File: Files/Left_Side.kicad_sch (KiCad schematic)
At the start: 76 parts, among them J1 USB_C_Receptacle, J3 USB_C_Receptacle, U1 W25Q128JVS, U2 XC6206-3.3_SOT, U3 USBLC6-2SC6, U4 RP2040, Y1 Crystal_GND24

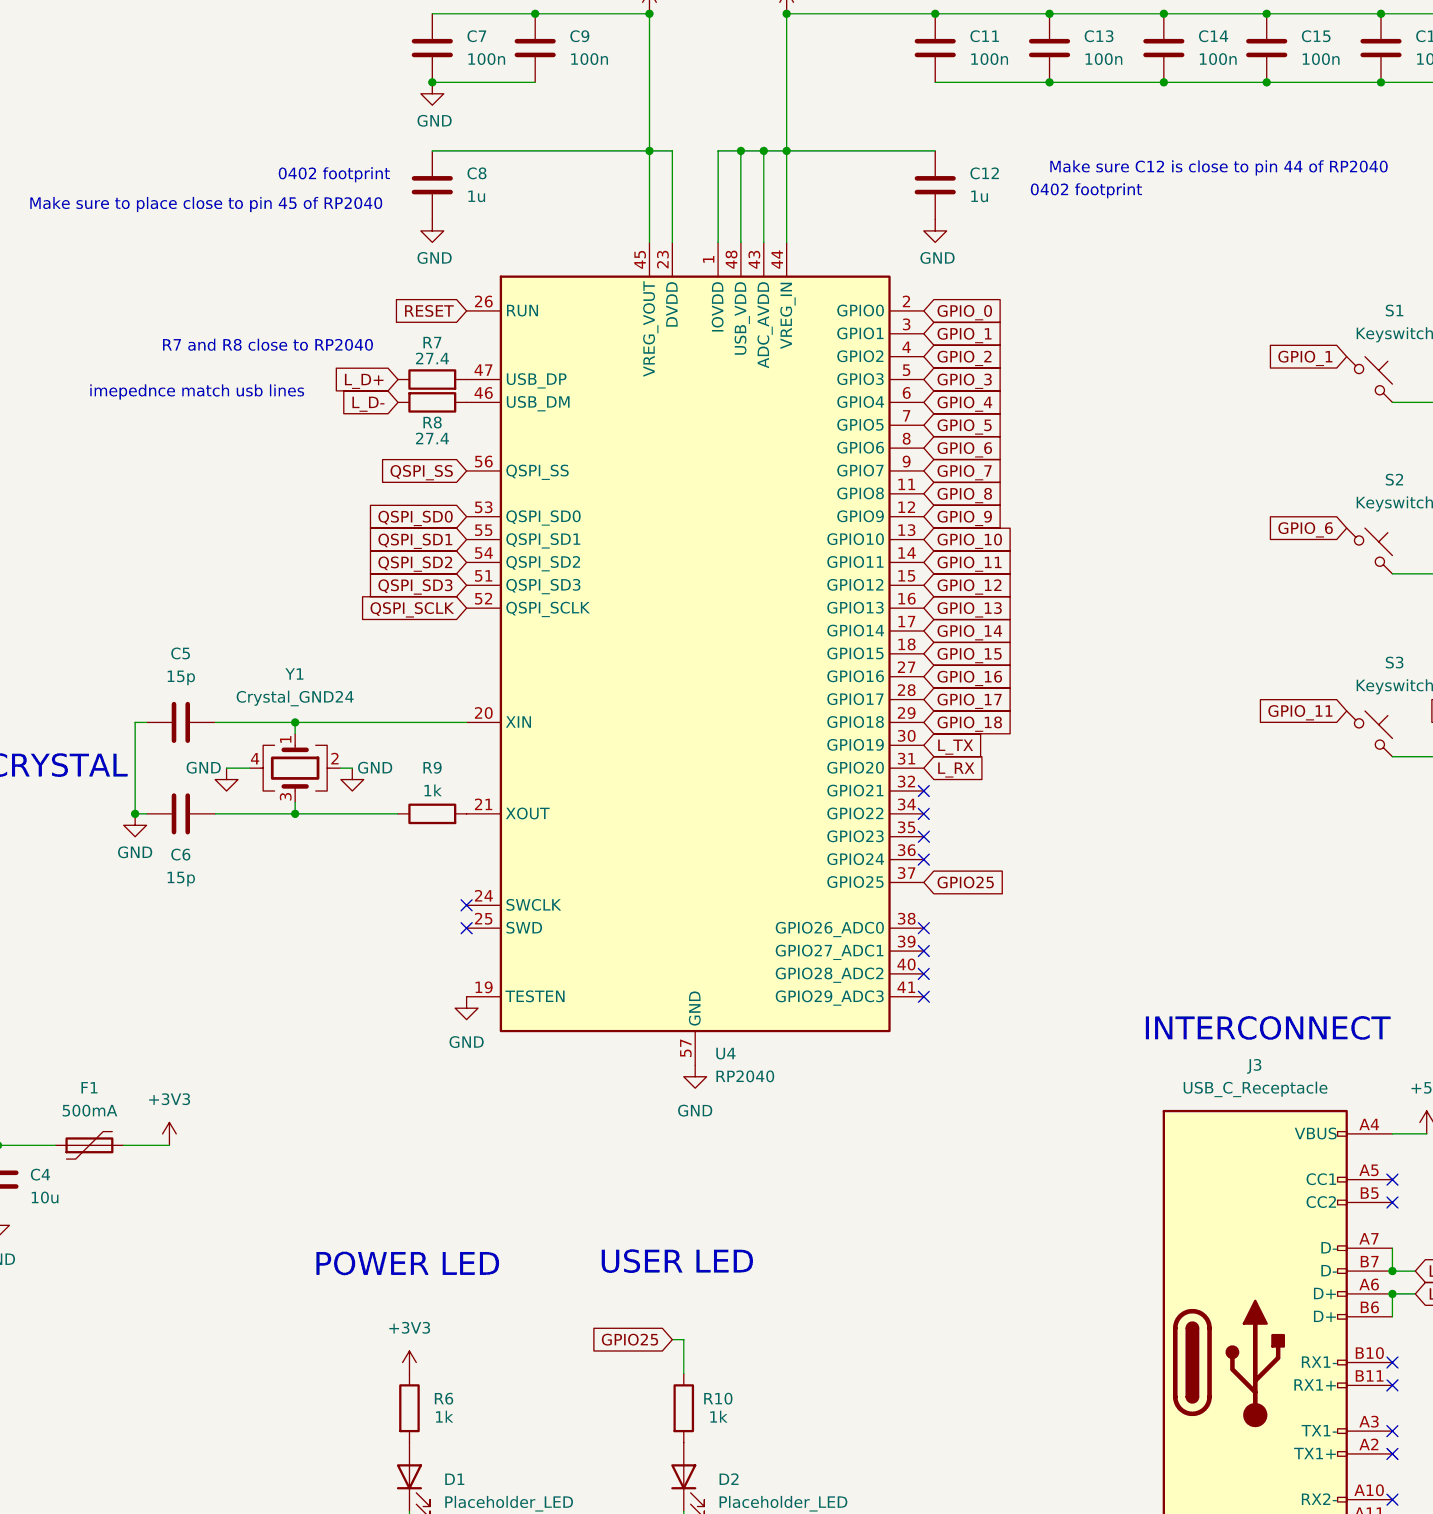
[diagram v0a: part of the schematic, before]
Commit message: placed companets and semi routed
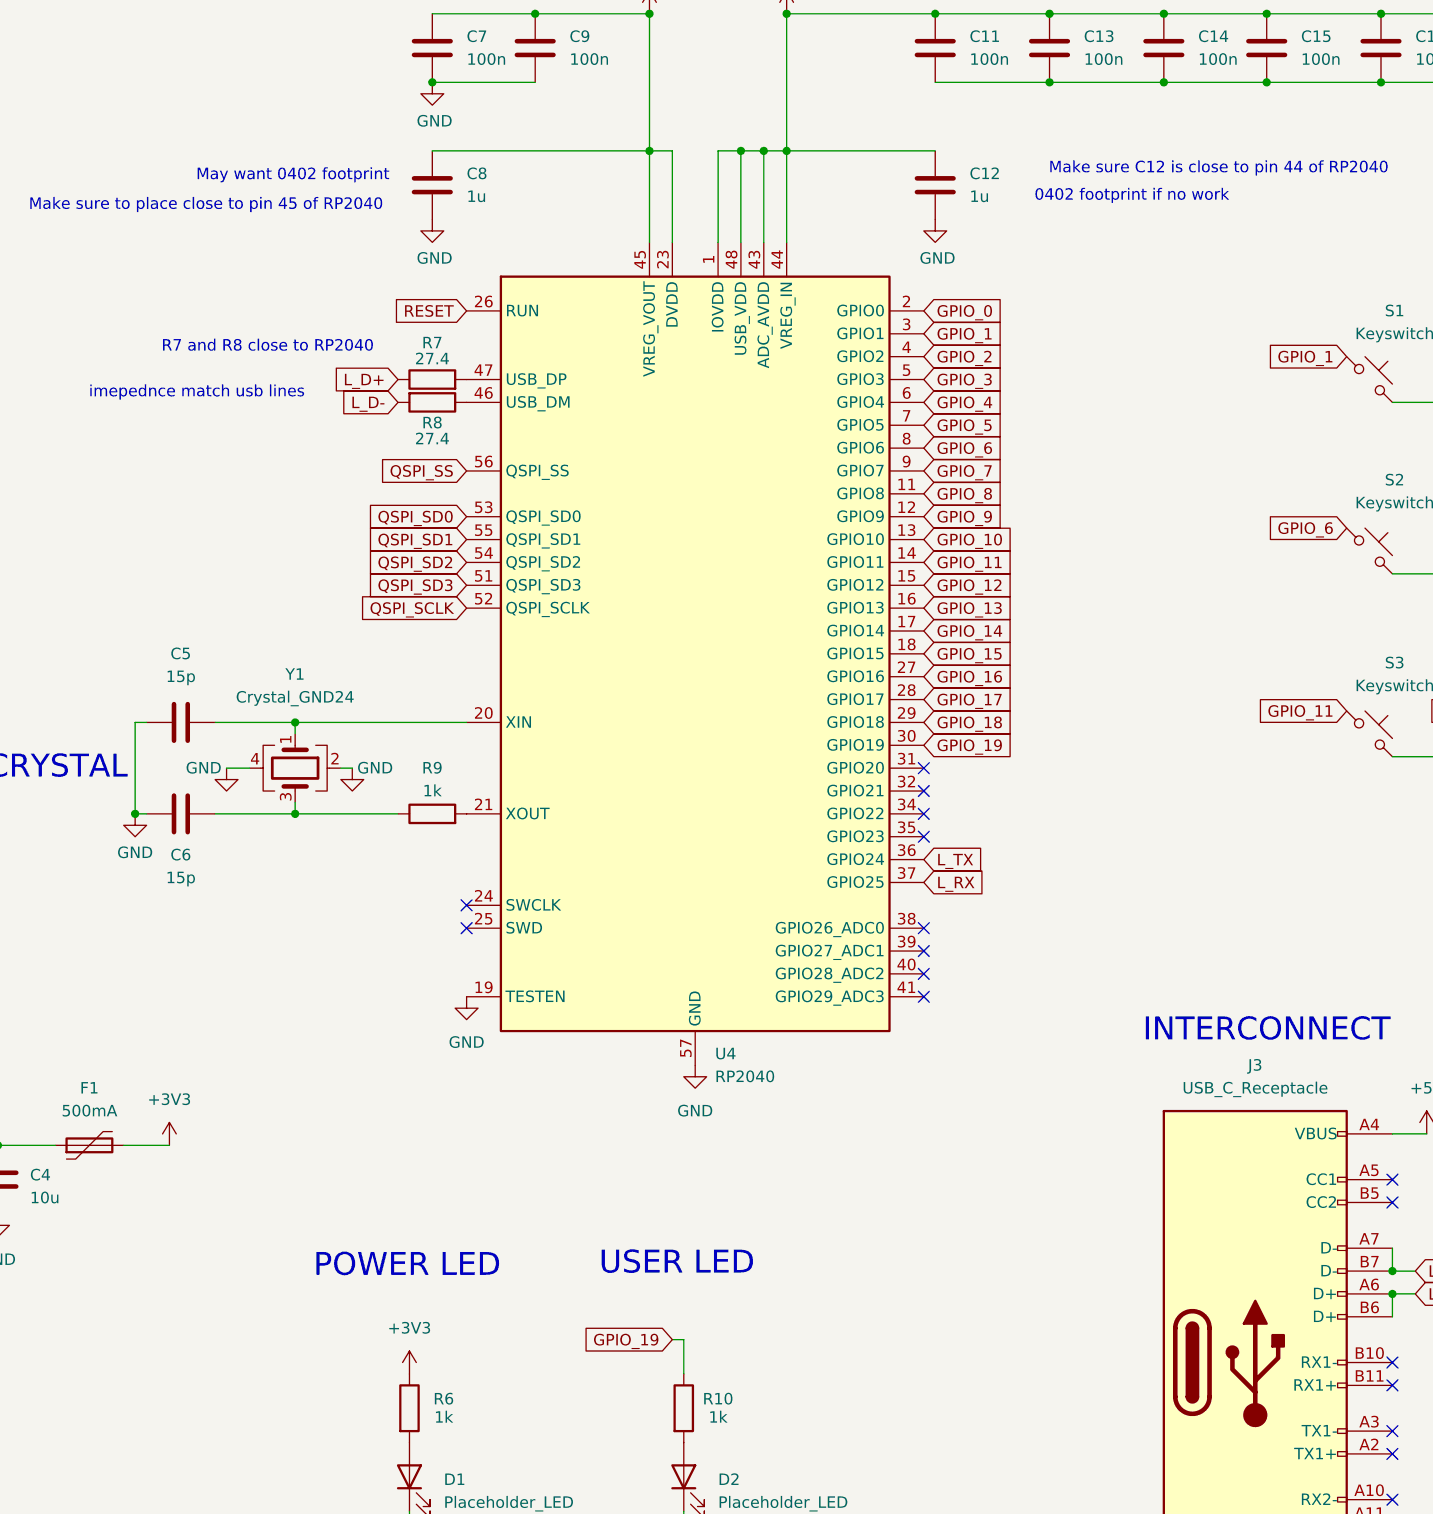
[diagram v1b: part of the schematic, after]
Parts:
- C1, C10, C11, C13, C14, C15, C16, C17, C18, C2, C3, C4, C5, C6, C7, C9: footprint ScottoKeebs_Components:Capacitor_0603 -> Capacitor_SMD:C_0805_2012Metric_Pad1.18x1.45mm_HandSolder
- C12, C8: footprint ScottoKeebs_Components:Capacitor_0402 -> Capacitor_SMD:C_0805_2012Metric_Pad1.18x1.45mm_HandSolder
- R1, R10, R2, R3, R4, R5, R6, R7, R8, R9: footprint Resistor_SMD:R_0603_1608Metric -> Resistor_SMD:R_0805_2012Metric_Pad1.20x1.40mm_HandSolder
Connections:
- net L_RX: now also U4.37 (GPIO25); no longer U4.31 (GPIO20)
- net L_TX: now also U4.36 (GPIO24); no longer U4.30 (GPIO19)
- net GPIO25 renamed GPIO_19
- net GPIO_19: now also U4.30 (GPIO19); no longer U4.37 (GPIO25)
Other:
- note added: "0402 footprint if no work"
- note added: "May want 0402 footprint"
- note removed: "0402 footprint"
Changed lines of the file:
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@@
 	)
 	(no_connect
-		(at 240.03 147.32)
-	)
-	(no_connect
 		(at 292.1 220.98)
 	)
@@
 	)
 	(no_connect
+		(at 240.03 137.16)
+	)
+	(no_connect
 		(at 83.82 234.95)
 	)
@@
 		)
 	)
-	(text "0402 footprint\n"
+	(text "May want 0402 footprint\n"
 		(exclude_from_sim no)
-		(at 174.498 71.374 0)
+		(at 169.926 71.374 0)
 		(effects
 			(font
@@
 		)
 	)
-	(text "0402 footprint\n"
+	(text "0402 footprint if no work\n"
 		(exclude_from_sim no)
-		(at 258.064 73.152 0)
+		(at 263.144 73.66 0)
 		(effects
 			(font
@@
 		)
 	)
-	(global_label "GPIO25"
+	(global_label "GPIO_19"
 		(shape input)
-		(at 240.03 149.86 0)
+		(at 240.03 134.62 0)
 		(fields_autoplaced yes)
 		(effects
@@
 		)
 		(property "Intersheetrefs" "${INTERSHEET_REFS}"
-			(at 249.9095 149.86 0)
+			(at 250.8771 134.62 0)
 			(effects
 				(font
@@
 		)
 	)
-	(global_label "GPIO25"
+	(global_label "GPIO_19"
 		(shape input)
 		(at 212.09 200.66 180)
@@
 		)
 		(property "Intersheetrefs" "${INTERSHEET_REFS}"
-			(at 202.2105 200.66 0)
+			(at 201.2429 200.66 0)
 			(effects
 				(font
@@
 	(global_label "L_TX"
 		(shape input)
-		(at 240.03 134.62 0)
+		(at 240.03 147.32 0)
 		(fields_autoplaced yes)
 		(effects
@@
 		)
 		(property "Intersheetrefs" "${INTERSHEET_REFS}"
-			(at 247.188 134.62 0)
+			(at 247.188 147.32 0)
 			(effects
 				(font
@@
 	(global_label "L_RX"
 		(shape input)
-		(at 240.03 137.16 0)
+		(at 240.03 149.86 0)
 		(fields_autoplaced yes)
 		(effects
@@
 		)
 		(property "Intersheetrefs" "${INTERSHEET_REFS}"
-			(at 247.4904 137.16 0)
+			(at 247.4904 149.86 0)
 			(effects
 				(font
@@
 			)
 		)
-		(property "Footprint" "ScottoKeebs_Components:Capacitor_0603"
+		(property "Footprint" "Capacitor_SMD:C_0805_2012Metric_Pad1.18x1.45mm_HandSolder"
 			(at 153.67 133.0452 0)
 			(effects
@@
 			)
 		)
-		(property "Footprint" "Resistor_SMD:R_0603_1608Metric"
+		(property "Footprint" "Resistor_SMD:R_0805_2012Metric_Pad1.20x1.40mm_HandSolder"
 			(at 87.63 185.928 90)
 			(effects
@@
 			)
 		)
-		(property "Footprint" "ScottoKeebs_Components:Capacitor_0603"
+		(property "Footprint" "Capacitor_SMD:C_0805_2012Metric_Pad1.18x1.45mm_HandSolder"
 			(at 138.1252 186.69 0)
 			(effects
@@
 			)
 		)
-		(property "Footprint" "ScottoKeebs_Components:Capacitor_0603"
+		(property "Footprint" "Capacitor_SMD:C_0805_2012Metric_Pad1.18x1.45mm_HandSolder"
 			(at 84.1248 57.15 0)
 			(effects
@@
 			)
 		)
-		(property "Footprint" "Resistor_SMD:R_0603_1608Metric"
+		(property "Footprint" "Resistor_SMD:R_0805_2012Metric_Pad1.20x1.40mm_HandSolder"
 			(at 185.42 144.018 90)
 			(effects
@@
 			)
 		)
-		(property "Footprint" "ScottoKeebs_Components:Capacitor_0402"
+		(property "Footprint" "Capacitor_SMD:C_0805_2012Metric_Pad1.18x1.45mm_HandSolder"
 			(at 186.3852 76.2 0)
 			(effects
@@
 			)
 		)
-		(property "Footprint" "ScottoKeebs_Components:Capacitor_0603"
+		(property "Footprint" "Capacitor_SMD:C_0805_2012Metric_Pad1.18x1.45mm_HandSolder"
 			(at 279.0952 60.96 0)
 			(effects
@@
 			)
 		)
-		(property "Footprint" "ScottoKeebs_Components:Capacitor_0603"
+		(property "Footprint" "Capacitor_SMD:C_0805_2012Metric_Pad1.18x1.45mm_HandSolder"
 			(at 186.3852 60.96 0)
 			(effects
@@
 			)
 		)
-		(property "Footprint" "Resistor_SMD:R_0603_1608Metric"
+		(property "Footprint" "Resistor_SMD:R_0805_2012Metric_Pad1.20x1.40mm_HandSolder"
 			(at 185.42 95.758 90)
 			(effects
@@
 			)
 		)
-		(property "Footprint" "ScottoKeebs_Components:Capacitor_0603"
+		(property "Footprint" "Capacitor_SMD:C_0805_2012Metric_Pad1.18x1.45mm_HandSolder"
 			(at 121.92 105.7148 0)
 			(effects
@@
 			)
 		)
-		(property "Footprint" "ScottoKeebs_Components:Capacitor_0603"
+		(property "Footprint" "Capacitor_SMD:C_0805_2012Metric_Pad1.18x1.45mm_HandSolder"
 			(at 153.67 143.2052 0)
 			(effects
@@
 			)
 		)
-		(property "Footprint" "ScottoKeebs_Components:Capacitor_0603"
+		(property "Footprint" "Capacitor_SMD:C_0805_2012Metric_Pad1.18x1.45mm_HandSolder"
 			(at 318.4652 60.96 0)
 			(effects
@@
 			)
 		)
-		(property "Footprint" "ScottoKeebs_Components:Capacitor_0603"
+		(property "Footprint" "Capacitor_SMD:C_0805_2012Metric_Pad1.18x1.45mm_HandSolder"
 			(at 105.1052 186.69 0)
 			(effects
@@
 			)
 		)
-		(property "Footprint" "ScottoKeebs_Components:Capacitor_0603"
+		(property "Footprint" "Capacitor_SMD:C_0805_2012Metric_Pad1.18x1.45mm_HandSolder"
 			(at 304.4952 60.96 0)
 			(effects
@@
 			)
 		)
-		(property "Footprint" "ScottoKeebs_Components:Capacitor_0603"
+		(property "Footprint" "Capacitor_SMD:C_0805_2012Metric_Pad1.18x1.45mm_HandSolder"
 			(at 267.6652 60.96 0)
 			(effects
@@
 			)
 		)
-		(property "Footprint" "ScottoKeebs_Components:Capacitor_0603"
+		(property "Footprint" "Capacitor_SMD:C_0805_2012Metric_Pad1.18x1.45mm_HandSolder"
 			(at 254.9652 60.96 0)
 			(effects
@@
 			)
 		)
-		(property "Footprint" "ScottoKeebs_Components:Capacitor_0603"
+		(property "Footprint" "Capacitor_SMD:C_0805_2012Metric_Pad1.18x1.45mm_HandSolder"
 			(at 197.8152 60.96 0)
 			(effects
@@
 			)
 		)
-		(property "Footprint" "ScottoKeebs_Components:Capacitor_0402"
+		(property "Footprint" "Capacitor_SMD:C_0805_2012Metric_Pad1.18x1.45mm_HandSolder"
 			(at 242.2652 76.2 0)
 			(effects
@@
 			)
 		)
-		(property "Footprint" "ScottoKeebs_Components:Capacitor_0603"
+		(property "Footprint" "Capacitor_SMD:C_0805_2012Metric_Pad1.18x1.45mm_HandSolder"
 			(at 240.9952 41.91 0)
 			(effects
@@
 			)
 		)
-		(property "Footprint" "Resistor_SMD:R_0603_1608Metric"
+		(property "Footprint" "Resistor_SMD:R_0805_2012Metric_Pad1.20x1.40mm_HandSolder"
 			(at 185.42 94.742 90)
 			(effects
@@
 			)
 		)
-		(property "Footprint" "Resistor_SMD:R_0603_1608Metric"
+		(property "Footprint" "Resistor_SMD:R_0805_2012Metric_Pad1.20x1.40mm_HandSolder"
 			(at 87.63 188.468 90)
 			(effects
@@
 			)
 		)
-		(property "Footprint" "Resistor_SMD:R_0603_1608Metric"
+		(property "Footprint" "Resistor_SMD:R_0805_2012Metric_Pad1.20x1.40mm_HandSolder"
 			(at 95.758 110.49 90)
 			(effects
@@
 			)
 		)
-		(property "Footprint" "ScottoKeebs_Components:Capacitor_0603"
+		(property "Footprint" "Capacitor_SMD:C_0805_2012Metric_Pad1.18x1.45mm_HandSolder"
 			(at 291.7952 60.96 0)
 			(effects
@@
 			)
 		)
-		(property "Footprint" "Resistor_SMD:R_0603_1608Metric"
+		(property "Footprint" "Resistor_SMD:R_0805_2012Metric_Pad1.20x1.40mm_HandSolder"
 			(at 211.582 208.28 90)
 			(effects
@@
 			)
 		)
-		(property "Footprint" "ScottoKeebs_Components:Capacitor_0603"
+		(property "Footprint" "Capacitor_SMD:C_0805_2012Metric_Pad1.18x1.45mm_HandSolder"
 			(at 242.2652 60.96 0)
 			(effects
@@
 			)
 		)
-		(property "Footprint" "Resistor_SMD:R_0603_1608Metric"
+		(property "Footprint" "Resistor_SMD:R_0805_2012Metric_Pad1.20x1.40mm_HandSolder"
 			(at 76.962 50.8 90)
 			(effects
@@
 			)
 		)
-		(property "Footprint" "Resistor_SMD:R_0603_1608Metric"
+		(property "Footprint" "Resistor_SMD:R_0805_2012Metric_Pad1.20x1.40mm_HandSolder"
 			(at 85.09 113.538 90)
 			(effects
@@
 			)
 		)
-		(property "Footprint" "Resistor_SMD:R_0603_1608Metric"
+		(property "Footprint" "Resistor_SMD:R_0805_2012Metric_Pad1.20x1.40mm_HandSolder"
 			(at 181.102 208.28 90)
 			(effects
